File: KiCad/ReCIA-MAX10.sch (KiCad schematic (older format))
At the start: 18 parts, among them J1 Conn_02x03_Odd_Even, U1 AMS1117-3.3, U2 SN74CBT16210, U3 SN74CBT16210, U4 10M02SCU169, U5 8520_DIP_SOCKET, X1 Oscillator_3.2x2.5mm-28.6363M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

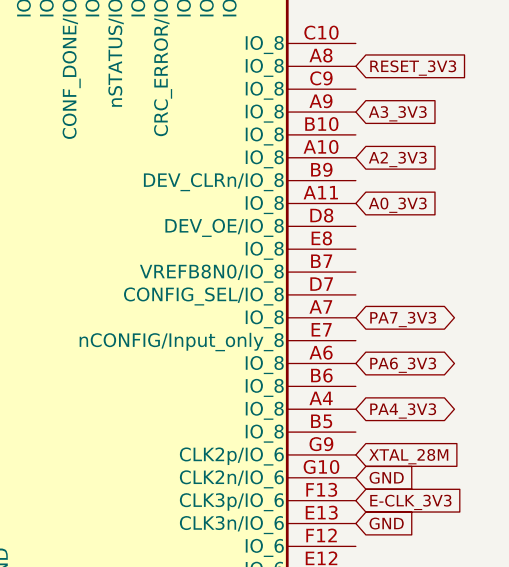
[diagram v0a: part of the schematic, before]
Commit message: Add pin assignment and routing for D0,D1,D2 to the FPGA
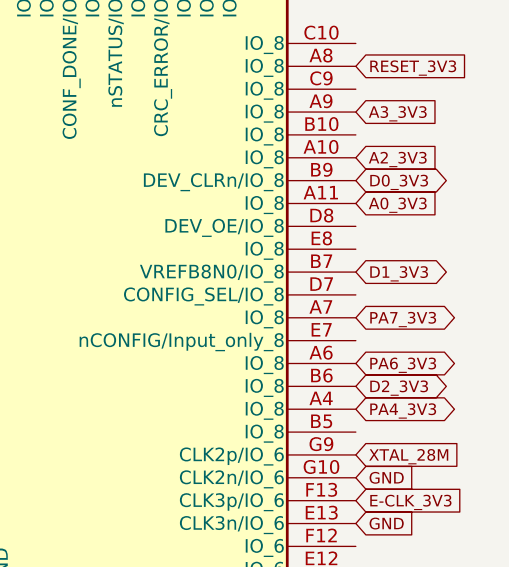
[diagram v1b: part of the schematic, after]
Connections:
- net D0_3V3: now also U4.B9 (DEV_CLRn/IO_8)
- net D1_3V3: now also U4.B7 (VREFB8N0/IO_8)
- net D2_3V3: now also U4.B6 (IO_8)
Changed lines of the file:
@@
 Text GLabel 9300 1050 1    50   BiDi ~ 0
 PA2_3V3
+Text GLabel 10650 2250 2    50   BiDi ~ 0
+D0_3V3
+Text GLabel 10650 2650 2    50   BiDi ~ 0
+D1_3V3
+Text GLabel 10650 3150 2    50   BiDi ~ 0
+D2_3V3
 $EndSCHEMATC

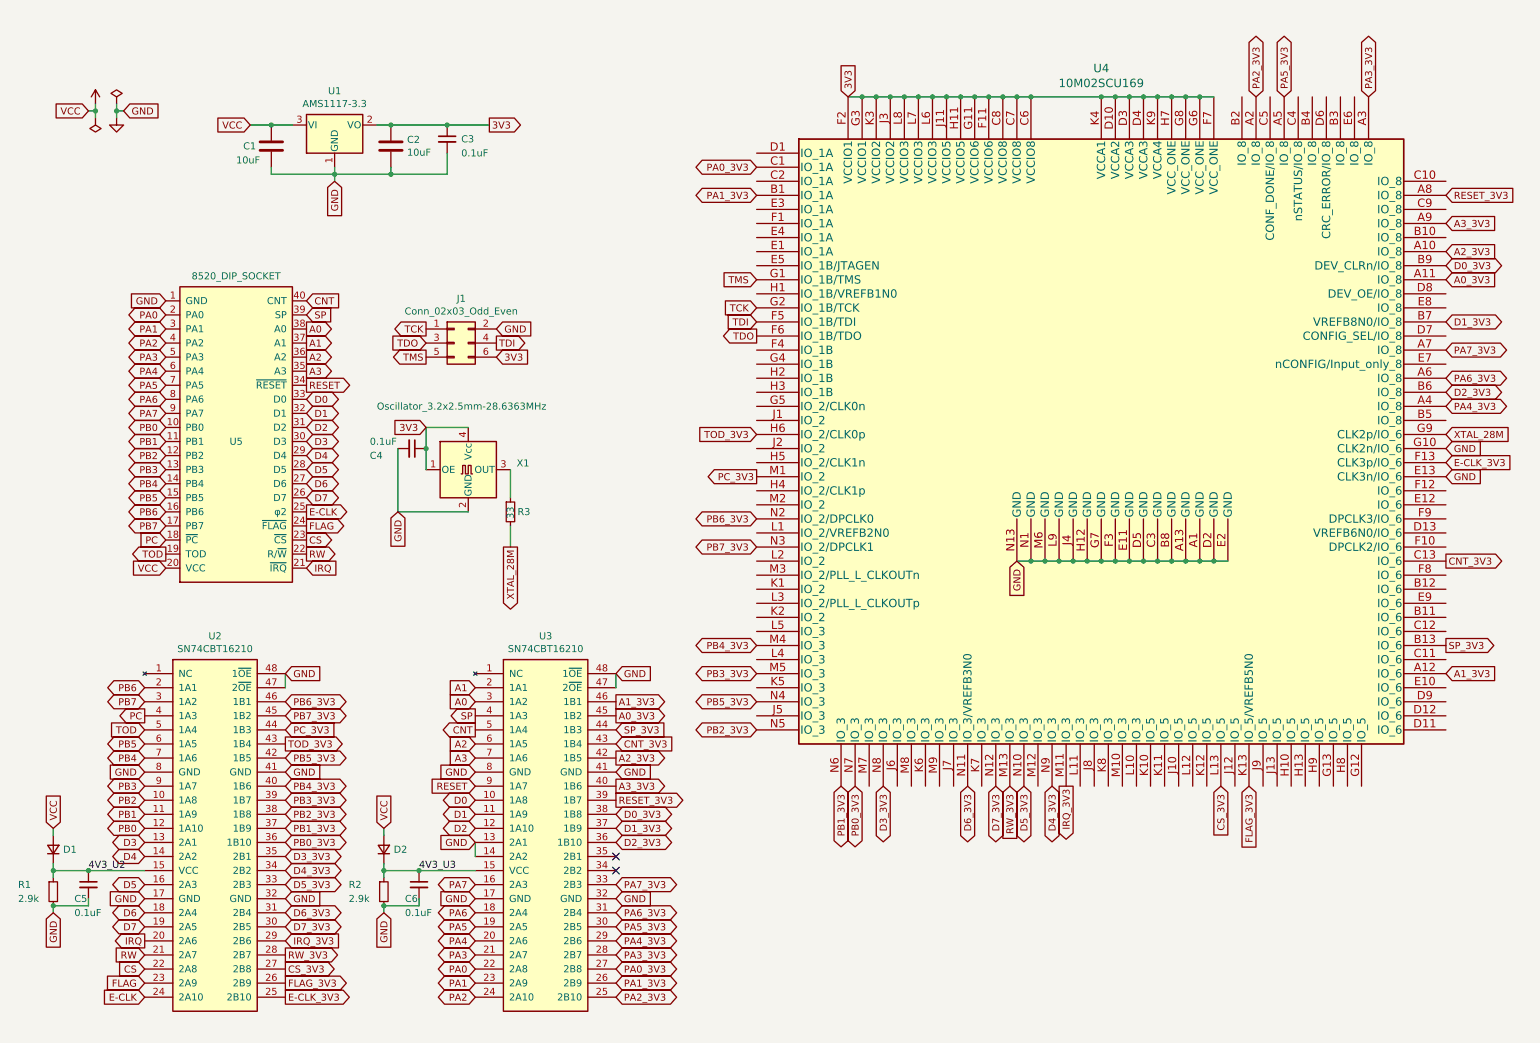
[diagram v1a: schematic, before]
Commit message: Add decoupling caps for FPGA-chip
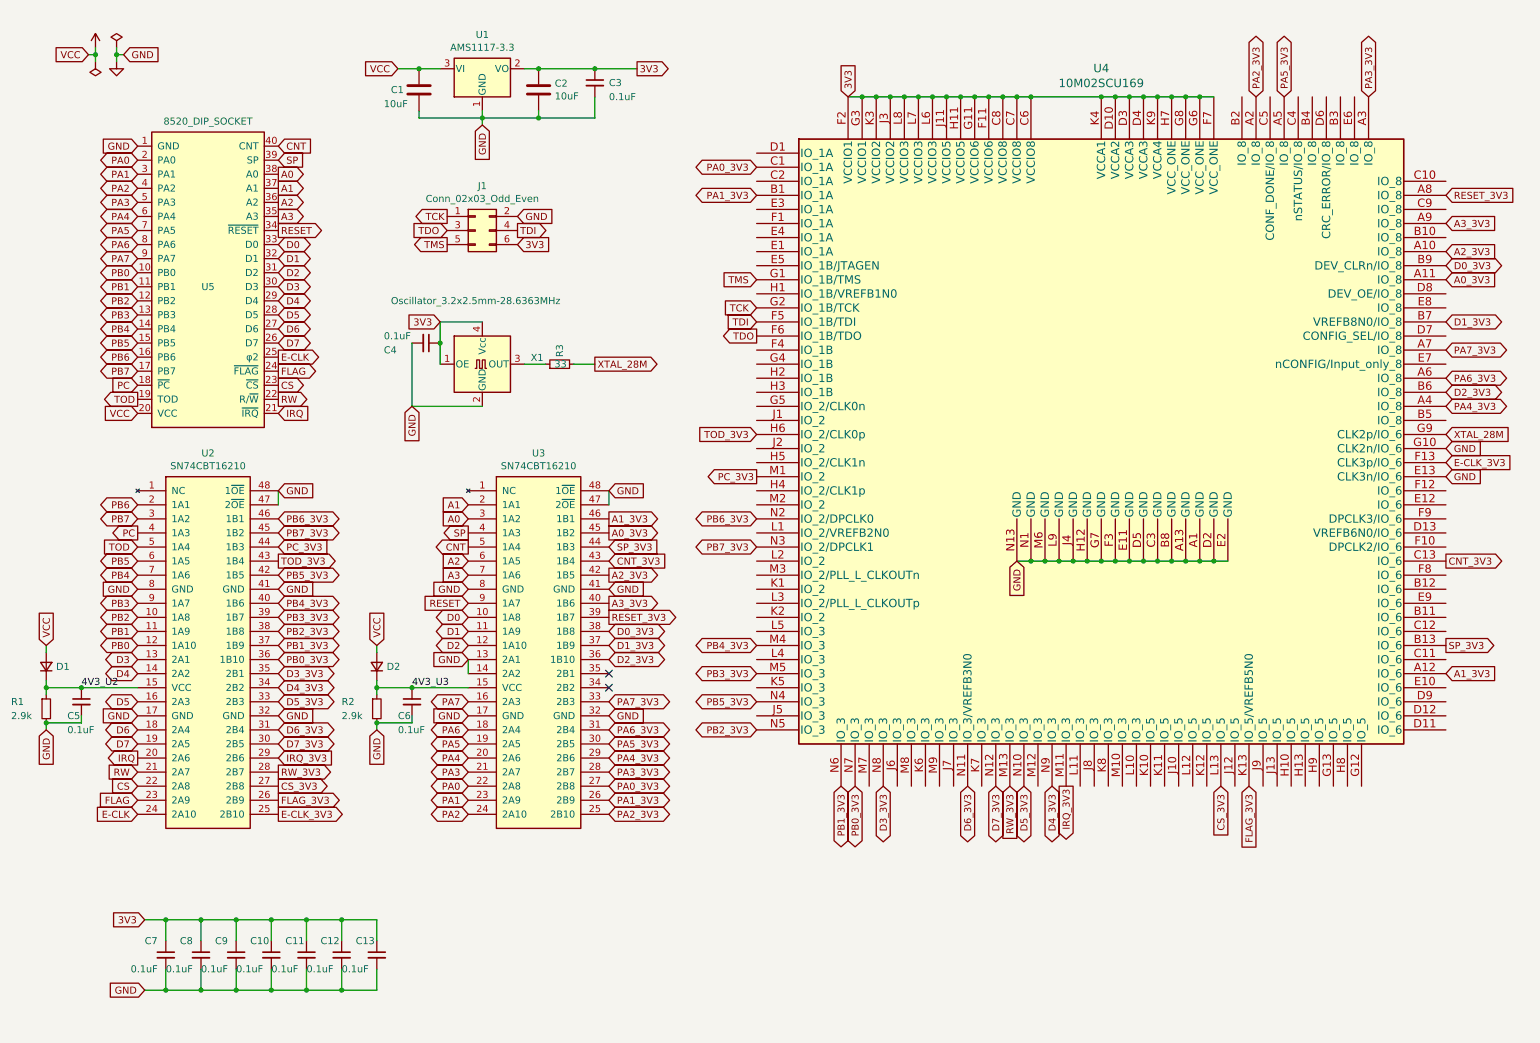
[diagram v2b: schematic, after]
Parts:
- added C10, C11, C12, C13, C7, C8, C9: 0.1uF, Capacitor_SMD:C_0603_1608Metric_Pad1.08x0.95mm_HandSolder, symbol Device:C_Small
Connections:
- net 3V3: now also C10.1, C11.1, C12.1, C13.1, C7.1, C8.1, C9.1
- net GND: now also C10.2, C11.2, C12.2, C13.2, C7.2, C8.2, C9.2
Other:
- moved on the sheet: C1, C2, C3, C4, C5, C6, D1, D2, J1, R1, R2, R3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

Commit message: Add more decoupling caps for FPGA-chip
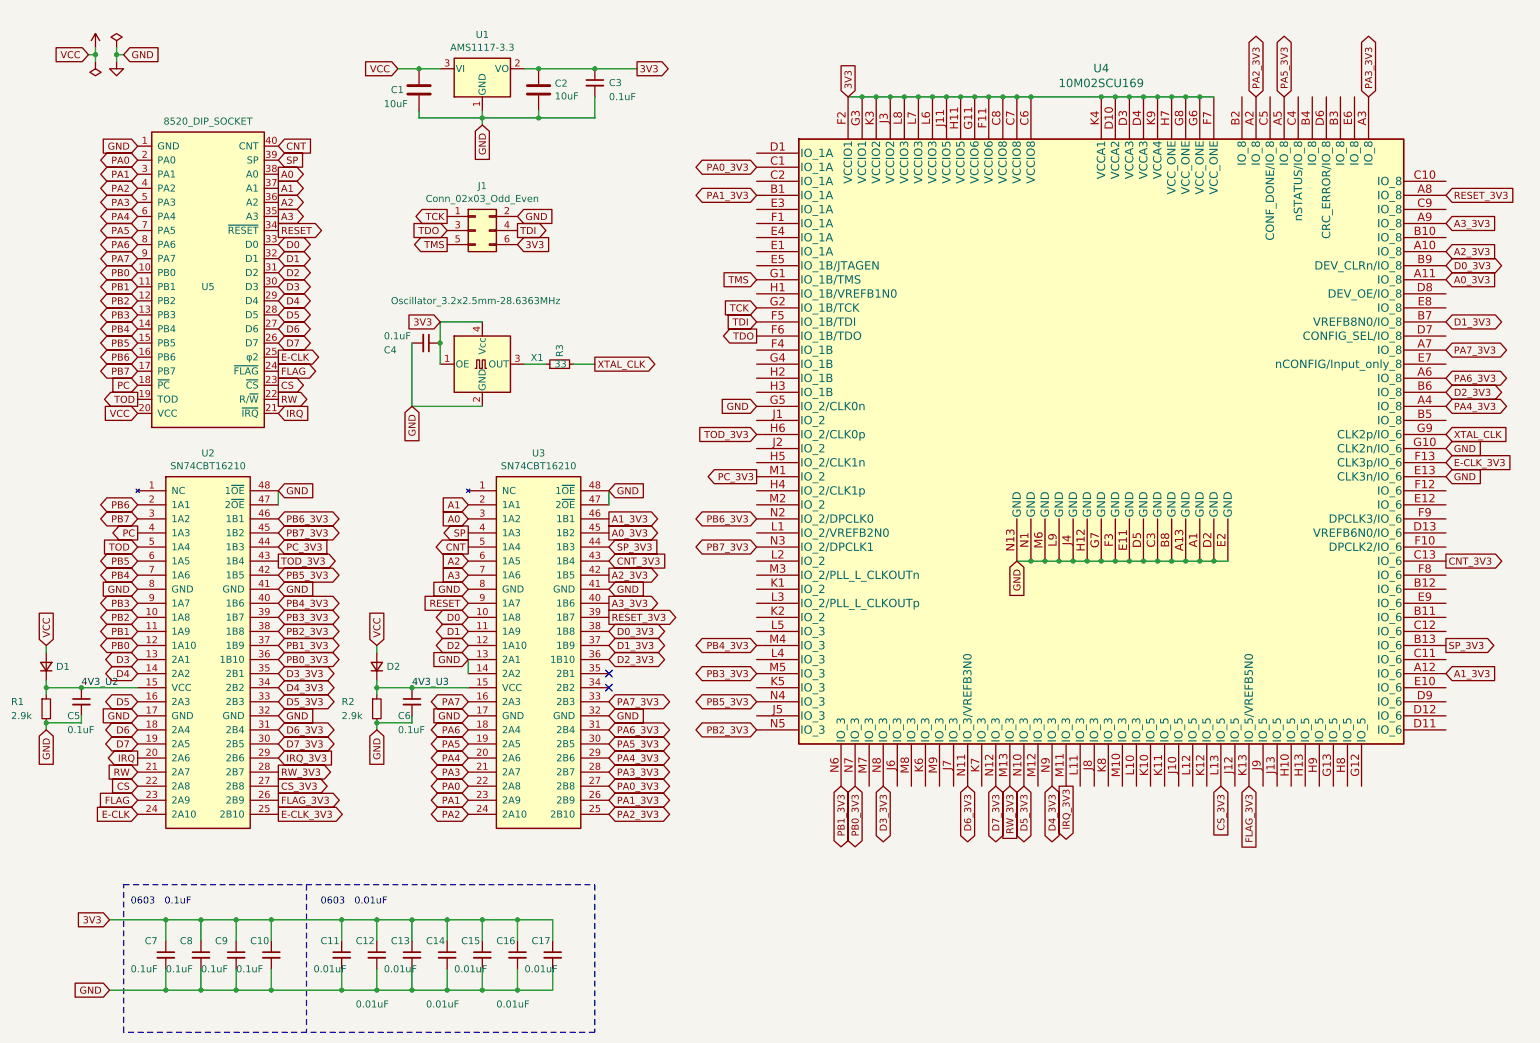
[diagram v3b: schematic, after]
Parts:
- added C10: 0.1uF, Capacitor_SMD:C_0603_1608Metric, symbol Device:C_Small
- added C13: 0.01uF, Capacitor_SMD:C_0603_1608Metric_Pad1.08x0.95mm_HandSolder, symbol Device:C_Small
- added C16, C17: 0.01uF, Capacitor_SMD:C_0603_1608Metric, symbol Device:C_Small
- C11: renamed from C9; value 0.1uF -> 0.01uF
- C12: renamed from C11; value 0.1uF -> 0.01uF
- C14: renamed from C8; value 0.1uF -> 0.01uF
- C15: renamed from C13; value 0.1uF -> 0.01uF
- renumbered C10 to C7, C12 to C8, C7 to C9
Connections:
- net 3V3: now also C10.1, C13.1, C16.1, C17.1
- net GND: now also U4.G5 (IO_2/CLK0n), C10.2, C13.2, C16.2, C17.2
- net XTAL_28M renamed XTAL_CLK
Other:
- note added: "0603 0.01uF"
- note added: "0603 0.1uF"
- moved on the sheet: C11, C12, C14, C15, C7, C8, C9
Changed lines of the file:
@@
 GND
 Text GLabel 4600 2950 2    50   Output ~ 0
-XTAL_28M
+XTAL_CLK
 $Comp
 L Device:R_Small R3
@@
 $EndComp
 Text GLabel 10650 3450 2    50   Input ~ 0
-XTAL_28M
+XTAL_CLK
 Text GLabel 3700 4650 0    50   Input ~ 0
 RESET
@@
 	4450 2950 4600 2950
 $Comp
+L Device:C_Small C9
+U 1 1 67108887
+P 2050 7150
+F 0 "C9" H 1900 7250 50  0000 L CNN
+F 1 "0.1uF" H 1800 7050 50  0000 L CNN
+F 2 "Capacitor_SMD:C_0603_1608Metric_Pad1.08x0.95mm_HandSolder" H 2050 7150 50  0001 C CNN
+F 3 "~" H 2050 7150 50  0001 C CNN
+	1    2050 7150
+	1    0    0    -1
+$EndComp
+Text GLabel 1150 6900 0    50   Input ~ 0
+3V3
+Text GLabel 1150 7400 0    50   Input ~ 0
+GND
+Wire Wire Line
+	1550 7400 1550 7250
+Wire Wire Line
+	1550 6900 1550 7050
+$Comp
+L Device:C_Small C14
+U 1 1 6711F7C7
+P 3550 7150
+F 0 "C14" H 3400 7250 50  0000 L CNN
+F 1 "0.01uF" H 3400 6800 50  0000 L CNN
+F 2 "Capacitor_SMD:C_0603_1608Metric_Pad1.08x0.95mm_HandSolder" H 3550 7150 50  0001 C CNN
+F 3 "~" H 3550 7150 50  0001 C CNN
+	1    3550 7150
+	1    0    0    -1
+$EndComp
+Wire Wire Line
+	1800 7050 1800 6900
+Wire Wire Line
+	1800 6900 1550 6900
+Connection ~ 1550 6900
+Wire Wire Line
+	1550 7400 1800 7400
+Wire Wire Line
+	1800 7400 1800 7250
+Connection ~ 1550 7400
+$Comp
+L Device:C_Small C11
+U 1 1 671339B4
+P 2800 7150
+F 0 "C11" H 2650 7250 50  0000 L CNN
+F 1 "0.01uF" H 2600 7050 50  0000 L CNN
+F 2 "Capacitor_SMD:C_0603_1608Metric_Pad1.08x0.95mm_HandSolder" H 2800 7150 50  0001 C CNN
+F 3 "~" H 2800 7150 50  0001 C CNN
+	1    2800 7150
+	1    0    0    -1
+$EndComp
+$Comp
 L Device:C_Small C7
-U 1 1 67108887
+U 1 1 671339BE
 P 1550 7150
 F 0 "C7" H 1400 7250 50  0000 L CNN
@@
 	1    0    0    -1
 $EndComp
-Text GLabel 1400 6900 0    50   Input ~ 0
-3V3
-Text GLabel 1400 7400 0    50   Input ~ 0
-GND
-Wire Wire Line
-	1400 6900 1550 6900
-Wire Wire Line
-	1400 7400 1550 7400
-Wire Wire Line
-	1550 7400 1550 7250
-Wire Wire Line
-	1550 6900 1550 7050
+Wire Wire Line
+	1800 6900 2050 6900
+Wire Wire Line
+	2050 6900 2050 7050
+Connection ~ 1800 6900
+Wire Wire Line
+	1800 7400 2050 7400
+Wire Wire Line
+	2050 7400 2050 7250
+Connection ~ 1800 7400
+Wire Wire Line
+	2050 6900 2300 6900
+Wire Wire Line
+	2300 6900 2300 7050
+Connection ~ 2050 6900
+Wire Wire Line
+	2050 7400 2300 7400
+Wire Wire Line
+	2300 7400 2300 7250
+Connection ~ 2050 7400
+$Comp
+L Device:C_Small C12
+U 1 1 67152C37
+P 3050 7150
+F 0 "C12" H 2900 7250 50  0000 L CNN
+F 1 "0.01uF" H 2900 6800 50  0000 L CNN
+F 2 "Capacitor_SMD:C_0603_1608Metric_Pad1.08x0.95mm_HandSolder" H 3050 7150 50  0001 C CNN
+F 3 "~" H 3050 7150 50  0001 C CNN
+	1    3050 7150
+	1    0    0    -1
+$EndComp
 $Comp
 L Device:C_Small C8
-U 1 1 6711F7C7
+U 1 1 67152C41
 P 1800 7150
 F 0 "C8" H 1650 7250 50  0000 L CNN
@@
 $EndComp
 Wire Wire Line
-	1800 7050 1800 6900
-Wire Wire Line
-	1800 6900 1550 6900
-Connection ~ 1550 6900
-Wire Wire Line
-	1550 7400 1800 7400
-Wire Wire Line
-	1800 7400 1800 7250
-Connection ~ 1550 7400
-$Comp
-L Device:C_Small C9
-U 1 1 671339B4
-P 2050 7150
-F 0 "C9" H 1900 7250 50  0000 L CNN
-F 1 "0.1uF" H 1800 7050 50  0000 L CNN
-F 2 "Capacitor_SMD:C_0603_1608Metric_Pad1.08x0.95mm_HandSolder" H 2050 7150 50  0001 C CNN
-F 3 "~" H 2050 7150 50  0001 C CNN
-	1    2050 7150
+	2800 7400 2800 7250
+Wire Wire Line
+	3050 7400 3050 7250
+Wire Wire Line
+	2800 7050 2800 6900
+Connection ~ 2300 6900
+Wire Wire Line
+	3050 7050 3050 6900
+Connection ~ 2300 7400
+$Comp
+L Device:C_Small C15
+U 1 1 6718C019
+P 3800 7150
+F 0 "C15" H 3650 7250 50  0000 L CNN
+F 1 "0.01uF" H 3600 7050 50  0000 L CNN
+F 2 "Capacitor_SMD:C_0603_1608Metric_Pad1.08x0.95mm_HandSolder" H 3800 7150 50  0001 C CNN
+F 3 "~" H 3800 7150 50  0001 C CNN
+	1    3800 7150
+	1    0    0    -1
+$EndComp
+Wire Wire Line
+	3300 7050 3300 6900
+Wire Wire Line
+	3050 6900 2800 6900
+Connection ~ 2800 6900
+Wire Wire Line
+	3300 7250 3300 7400
+Wire Wire Line
+	3050 7400 2800 7400
+Connection ~ 2800 7400
+$Comp
+L Device:C_Small C13
+U 1 1 671A1C2C
+P 3300 7150
+F 0 "C13" H 3150 7250 50  0000 L CNN
+F 1 "0.01uF" H 3100 7050 50  0000 L CNN
+F 2 "Capacitor_SMD:C_0603_1608Metric_Pad1.08x0.95mm_HandSolder" H 3300 7150 50  0001 C CNN
+F 3 "~" H 3300 7150 50  0001 C CNN
+	1    3300 7150
+	1    0    0    -1
+$EndComp
+Wire Wire Line
+	3050 6900 3300 6900
+Wire Wire Line
+	3550 6900 3550 7050
+Connection ~ 3050 6900
+Wire Wire Line
+	3050 7400 3300 7400
+Wire Wire Line
+	3550 7400 3550 7250
+Connection ~ 3050 7400
+$Comp
+L Device:C_Small C16
+U 1 1 671B214C
+P 4050 7150
+F 0 "C16" H 3900 7250 50  0000 L CNN
+F 1 "0.01uF" H 3900 6800 50  0000 L CNN
+F 2 "Capacitor_SMD:C_0603_1608Metric" H 4050 7150 50  0001 C CNN
+F 3 "~" H 4050 7150 50  0001 C CNN
+	1    4050 7150
+	1    0    0    -1
+$EndComp
+Wire Wire Line
+	3300 6900 3550 6900
+Wire Wire Line
+	3800 6900 3800 7050
+Connection ~ 3300 6900
+Wire Wire Line
+	3300 7400 3550 7400
+Wire Wire Line
+	3800 7400 3800 7250
+Connection ~ 3300 7400
+$Comp
+L Device:C_Small C17
+U 1 1 671CA1F8
+P 4300 7150
+F 0 "C17" H 4150 7250 50  0000 L CNN
+F 1 "0.01uF" H 4100 7050 50  0000 L CNN
+F 2 "Capacitor_SMD:C_0603_1608Metric" H 4300 7150 50  0001 C CNN
+F 3 "~" H 4300 7150 50  0001 C CNN
+	1    4300 7150
 	1    0    0    -1
 $EndComp
 $Comp
 L Device:C_Small C10
-U 1 1 671339BE
+U 1 1 671CAB1F
 P 2300 7150
 F 0 "C10" H 2150 7250 50  0000 L CNN
 F 1 "0.1uF" H 2050 7050 50  0000 L CNN
-F 2 "Capacitor_SMD:C_0603_1608Metric_Pad1.08x0.95mm_HandSolder" H 2300 7150 50  0001 C CNN
+F 2 "Capacitor_SMD:C_0603_1608Metric" H 2300 7150 50  0001 C CNN
 F 3 "~" H 2300 7150 50  0001 C CNN
 	1    2300 7150
@@
 $EndComp
 Wire Wire Line
-	1800 6900 2050 6900
-Wire Wire Line
-	2050 6900 2050 7050
-Connection ~ 1800 6900
-Wire Wire Line
-	1800 7400 2050 7400
-Wire Wire Line
-	2050 7400 2050 7250
-Connection ~ 1800 7400
-Wire Wire Line
-	2050 6900 2300 6900
-Wire Wire Line
-	2300 6900 2300 7050
-Connection ~ 2050 6900
-Wire Wire Line
-	2050 7400 2300 7400
-Wire Wire Line
-	2300 7400 2300 7250
-Connection ~ 2050 7400
-$Comp
-L Device:C_Small C11
-U 1 1 67152C37
-P 2550 7150
-F 0 "C11" H 2400 7250 50  0000 L CNN
-F 1 "0.1uF" H 2300 7050 50  0000 L CNN
-F 2 "Capacitor_SMD:C_0603_1608Metric_Pad1.08x0.95mm_HandSolder" H 2550 7150 50  0001 C CNN
-F 3 "~" H 2550 7150 50  0001 C CNN
-	1    2550 7150
-	1    0    0    -1
-$EndComp
-$Comp
-L Device:C_Small C12
-U 1 1 67152C41
-P 2800 7150
-F 0 "C12" H 2650 7250 50  0000 L CNN
-F 1 "0.1uF" H 2550 7050 50  0000 L CNN
-F 2 "Capacitor_SMD:C_0603_1608Metric_Pad1.08x0.95mm_HandSolder" H 2800 7150 50  0001 C CNN
-F 3 "~" H 2800 7150 50  0001 C CNN
-	1    2800 7150
-	1    0    0    -1
-$EndComp
-Wire Wire Line
-	2550 7400 2550 7250
-Wire Wire Line
-	2800 7400 2800 7250
-Wire Wire Line
-	2550 7050 2550 6900
-Wire Wire Line
-	2550 6900 2300 6900
-Connection ~ 2300 6900
-Wire Wire Line
-	2800 7050 2800 6900
-Wire Wire Line
-	2800 6900 2550 6900
-Connection ~ 2550 6900
-Wire Wire Line
-	2550 7400 2300 7400
-Connection ~ 2300 7400
-Wire Wire Line
-	2800 7400 2550 7400
-Connection ~ 2550 7400
-$Comp
-L Device:C_Small C13
-U 1 1 6718C019
-P 3050 7150
-F 0 "C13" H 2900 7250 50  0000 L CNN
-F 1 "0.1uF" H 2800 7050 50  0000 L CNN
-F 2 "Capacitor_SMD:C_0603_1608Metric_Pad1.08x0.95mm_HandSolder" H 3050 7150 50  0001 C CNN
-F 3 "~" H 3050 7150 50  0001 C CNN
-	1    3050 7150
-	1    0    0    -1
-$EndComp
-Wire Wire Line
-	3050 7050 3050 6900
-Wire Wire Line
-	3050 6900 2800 6900
-Connection ~ 2800 6900
-Wire Wire Line
-	3050 7250 3050 7400
-Wire Wire Line
-	3050 7400 2800 7400
-Connection ~ 2800 7400
+	4050 7250 4050 7400
+Wire Wire Line
+	3800 7400 3550 7400
+Connection ~ 3550 7400
+Wire Wire Line
+	4050 7050 4050 6900
+Wire Wire Line
+	3800 6900 3550 6900
+Connection ~ 3550 6900
+Wire Wire Line
+	4300 7050 4300 6900
+Wire Wire Line
+	4050 6900 3800 6900
+Connection ~ 3800 6900
+Wire Wire Line
+	3800 7400 4050 7400
+Wire Wire Line
+	4300 7400 4300 7250
+Connection ~ 3800 7400
+Text GLabel 5750 3250 0    50   Input ~ 0
+GND
+Wire Wire Line
+	2300 6900 2800 6900
+Wire Wire Line
+	2300 7400 2800 7400
+Wire Wire Line
+	4050 6900 4300 6900
+Connection ~ 4050 6900
+Wire Wire Line
+	4050 7400 4300 7400
+Connection ~ 4050 7400
+Wire Wire Line
+	1150 6900 1550 6900
+Wire Wire Line
+	1150 7400 1550 7400
+Wire Notes Line
+	4600 6650 4600 7700
+Wire Notes Line
+	4600 7700 1250 7700
+Wire Notes Line
+	1250 7700 1250 6650
+Wire Notes Line
+	2550 6650 2550 7700
+Wire Notes Line
+	1250 6650 4600 6650
+Text Notes 1300 6800 0    50   ~ 0
+0603   0.1uF
+Text Notes 2650 6800 0    50   ~ 0
+0603   0.01uF
 $EndSCHEMATC
